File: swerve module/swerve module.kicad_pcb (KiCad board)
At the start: 2 copper layers, 63.5 x 37.2 mm, 9 parts, among them J1 MTJ-88ARX1-FSM-LG, J2 MTJ-88ARX1-FSM-LG, J3 CAN out, J4 12v, J5 CAN in, SW1 SW_DPST

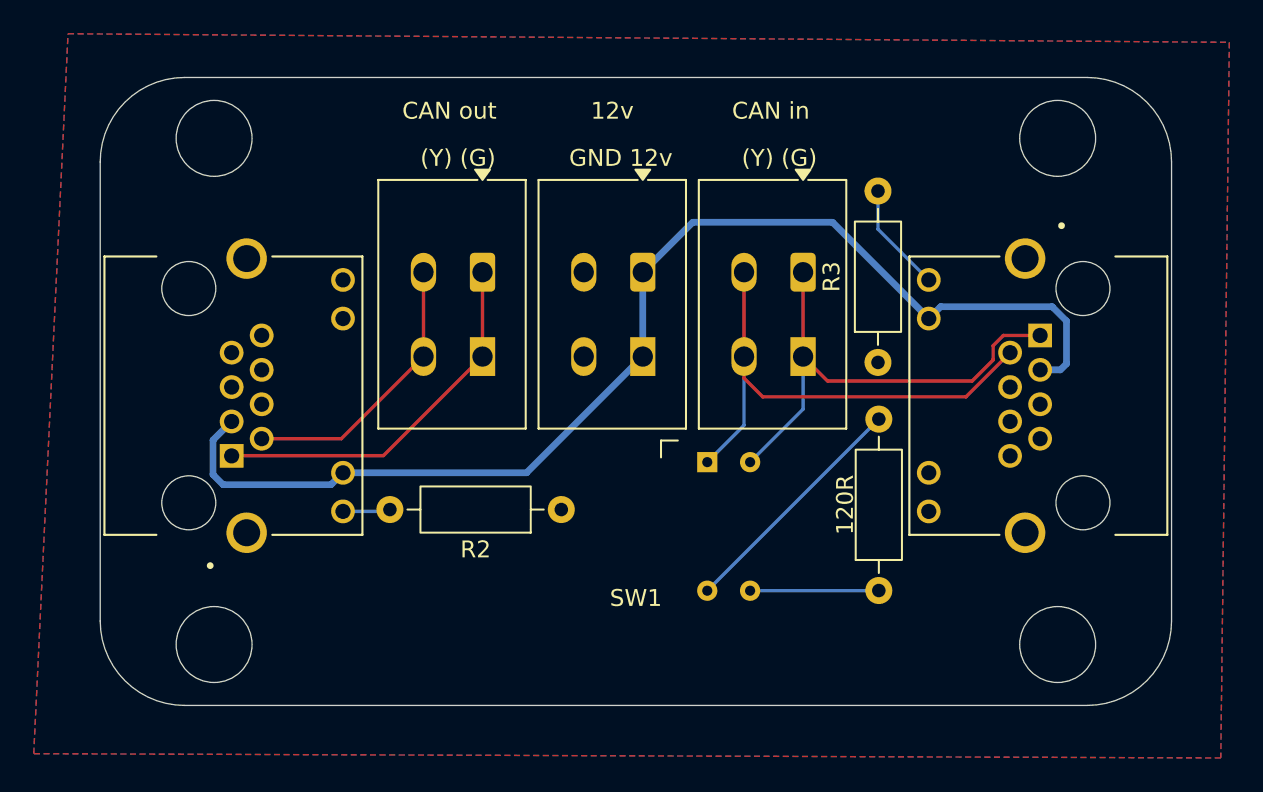
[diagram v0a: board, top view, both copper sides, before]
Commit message: rio module and added better silkscreening
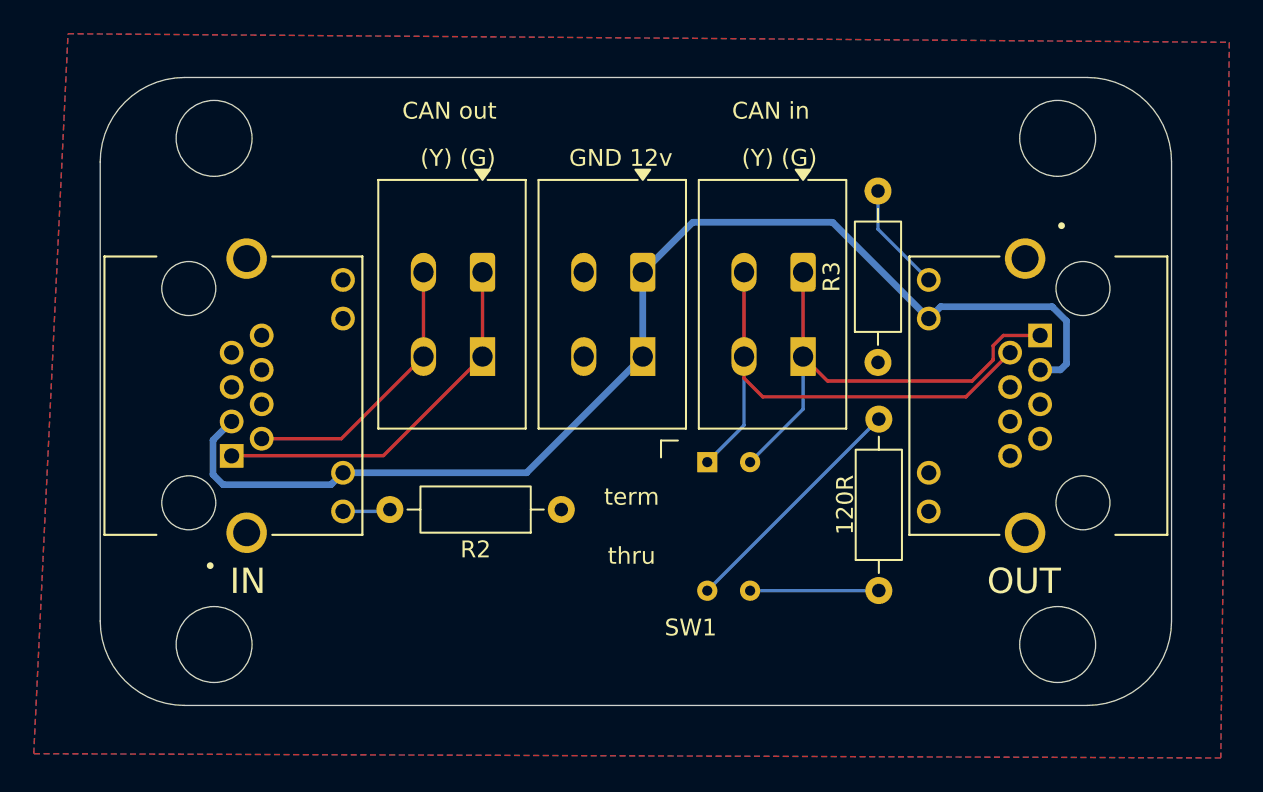
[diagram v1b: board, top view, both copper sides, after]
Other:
- board text added: "IN"
- board text added: "OUT"
- board text added: "term"
- board text added: "thru"
- board text removed: "12v"
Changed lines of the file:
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@@
 		)
 		(property "Value" "120R"
-			(at 5.08 1.25 90)
+			(at 5.05 0.1 90)
 			(layer "F.Fab")
 			(effects
@@
 			(fill no)
 			(layer "F.Fab")
-		)
-		(fp_text user "${REFERENCE}"
-			(at 5.08 0 90)
-			(layer "F.Fab")
-			(effects
-				(font
-					(size 1 1)
-					(thickness 0.15)
-				)
-			)
 		)
 		(pad "1" thru_hole circle
@@
 		(tags "tact sw push PVA1 DPST")
 		(property "Reference" "SW1"
-			(at -5.5 4.25 0)
+			(at -2.25 6 0)
 			(layer "F.SilkS")
 			(effects
@@
 		(layer "Edge.Cuts")
 	)
+	(gr_text "thru"
+		(at 102.75 65.75 0)
+		(layer "F.SilkS")
+		(effects
+			(font
+				(size 1 1)
+				(thickness 0.15)
+			)
+		)
+	)
+	(gr_text "OUT\n"
+		(at 126 67.25 0)
+		(layer "F.SilkS")
+		(effects
+			(font
+				(size 1.5 1.5)
+				(thickness 0.15)
+			)
+		)
+	)
 	(gr_text "(Y) (G)"
 		(at 111.506 42.164 0)
@@
 		)
 	)
+	(gr_text "term"
+		(at 102.75 62.25 0)
+		(layer "F.SilkS")
+		(effects
+			(font
+				(size 1 1)
+				(thickness 0.15)
+			)
+		)
+	)
 	(gr_text "GND 12v"
 		(at 102.108 42.164 0)
@@
 		)
 	)
-	(gr_text "12v"
-		(at 101.6 39.37 0)
-		(layer "F.SilkS")
-		(effects
-			(font
-				(size 1 1)
-				(thickness 0.15)
-			)
-		)
-	)
 	(gr_text "(Y) (G)"
 		(at 92.456 42.164 0)
@@
 		)
 	)
+	(gr_text "IN"
+		(at 80 67.25 0)
+		(layer "F.SilkS")
+		(effects
+			(font
+				(size 1.5 1.5)
+				(thickness 0.15)
+			)
+		)
+	)
 	(segment
 		(start 90.41 53.9325)
@@
 		(polygon
 			(pts
-				(xy 69.342 34.798) (xy 138.176 35.306) (xy 137.668 77.724) (xy 67.31 77.47) (xy 69.342 34.798)
-			)
-		)
+				(xy 69.342 34.798) (xy 138.176 35.306) (xy 137.668 77.724) (xy 67.31 77.47)
+			)
+		)

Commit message: final major changes, exported for JLCPCB
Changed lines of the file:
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@@
 		(tenting front back)
 		(pcbplotparams
-			(layerselection 0x00000000_00000000_55555555_5755f5ff)
+			(layerselection 0x00000000_00000000_55555555_575555ff)
 			(plot_on_all_layers_selection 0x00000000_00000000_00000000_00000000)
 			(disableapertmacros no)
-			(usegerberextensions no)
-			(usegerberattributes yes)
-			(usegerberadvancedattributes yes)
+			(usegerberextensions yes)
+			(usegerberattributes no)
+			(usegerberadvancedattributes no)
 			(creategerberjobfile yes)
 			(dashed_line_dash_ratio 12.000000)
@@
 			(plotframeref no)
 			(mode 1)
-			(useauxorigin no)
+			(useauxorigin yes)
 			(hpglpennumber 1)
 			(hpglpenspeed 20)
@@
 			(plotpadnumbers no)
 			(hidednponfab no)
-			(sketchdnponfab yes)
-			(crossoutdnponfab yes)
-			(subtractmaskfromsilk no)
+			(sketchdnponfab no)
+			(crossoutdnponfab no)
+			(subtractmaskfromsilk yes)
 			(outputformat 1)
 			(mirror no)
-			(drillshape 1)
+			(drillshape 0)
 			(scaleselection 1)
-			(outputdirectory "")
+			(outputdirectory "JLC/")
 		)
 	)
@@
 	)
 	(segment
-		(start 110.519 56.319)
+		(start 123.098 55.782)
+		(end 109.982 55.782)
+		(width 0.2)
+		(layer "F.Cu")
+		(net 6)
+	)
+	(segment
+		(start 109.982 55.782)
 		(end 109.41 55.21)
 		(width 0.2)
@@
 	)
 	(segment
-		(start 125.18 53.7)
-		(end 122.561 56.319)
-		(width 0.2)
-		(layer "F.Cu")
-		(net 6)
-	)
-	(segment
-		(start 122.561 56.319)
-		(end 110.519 56.319)
-		(width 0.2)
-		(layer "F.Cu")
-		(net 6)
-	)
-	(segment
 		(start 109.41 48.9325)
 		(end 109.41 53.9325)
 		(width 0.2)
 		(layer "F.Cu")
+		(net 6)
+	)
+	(segment
+		(start 125.18 53.7)
+		(end 123.098 55.782)
+		(width 0.2)
+		(layer "F.Cu")
